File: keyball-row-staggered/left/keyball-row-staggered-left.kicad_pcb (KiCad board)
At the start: 2 copper layers, 159.2 x 113.7 mm, 82 parts, among them J1 MJ-4PP-9, J10 Conn_01x01_Pin, J11 Conn_01x01_Pin, J12 Conn_01x01_Pin, J2 Conn_01x01_Pin, J3 Conn_01x01_Pin, J4 Conn_01x01_Pin, J5 Conn_01x01_Pin, J6 Conn_01x01_Pin, J7 Conn_01x01_Pin, J8 Conn_01x01_Pin, J9 Conn_01x01_Pin, SW1 SW_PUSH, SW10 SW_PUSH, SW11 SW_PUSH, SW12 SW_PUSH, SW13 SW_PUSH, SW14 SW_PUSH, SW15 SW_PUSH, SW16 SW_PUSH, SW17 SW_PUSH, SW18 SW_PUSH, SW19 SW_PUSH, SW2 SW_PUSH, SW20 SW_PUSH, SW21 SW_PUSH, SW22 SW_PUSH, SW23 SW_PUSH, SW24 SW_PUSH, SW25 SW_PUSH, SW26 SW_PUSH, SW27 SW_PUSH, SW28 SW_PUSH, SW29 SW_PUSH, SW3 SW_PUSH, SW30 SW_PUSH, SW31 SW_PUSH, SW4 SW_PUSH, SW5 SW_PUSH, SW6 SW_PUSH, SW7 SW_PUSH, SW8 SW_PUSH, SW9 SW_PUSH, U1 ProMicro

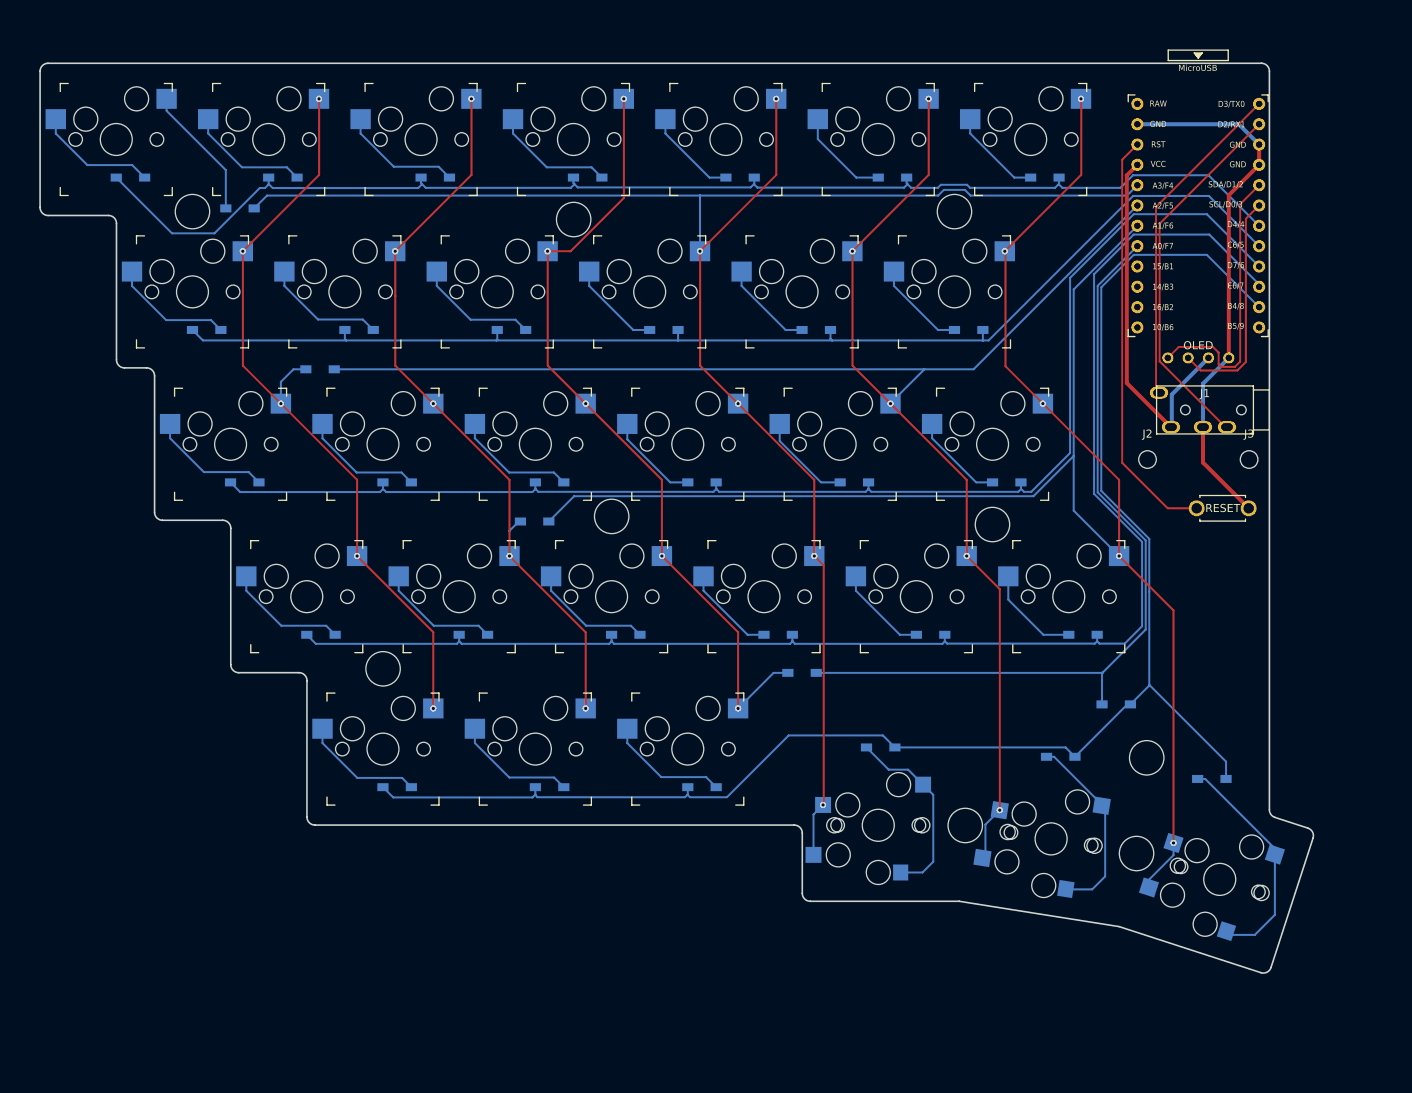
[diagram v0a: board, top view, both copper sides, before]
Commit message: add order-number placeholder
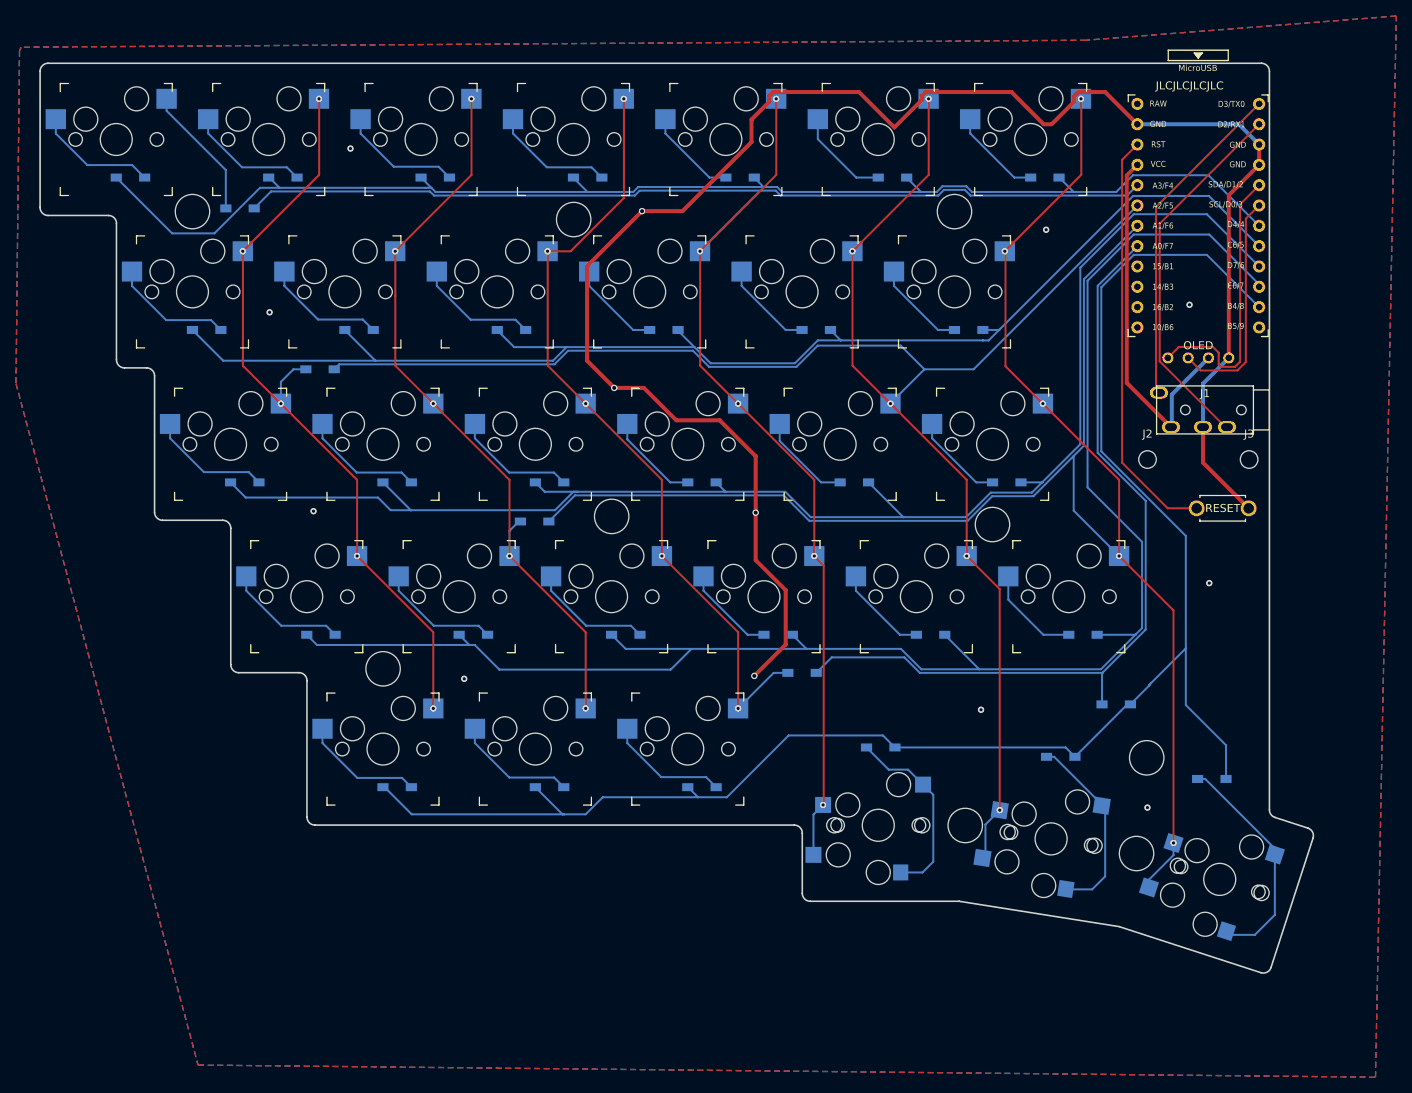
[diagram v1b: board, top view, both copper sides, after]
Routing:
- net GND: track 67.0 -> 224.7 mm, vias 0 -> 13
- net ROW3: track 183.2 -> 209.5 mm
- net ROW2: track 164.6 -> 184.8 mm
- net ROW1: track 150.7 -> 169.6 mm
- net ROW4: track 198.9 -> 211.7 mm
- net ROW0: track 159.1 -> 165.8 mm
- net COL0: track 224.5 -> 229.2 mm
- net COL1: track 222.3 -> 226.4 mm
- net COL2: track 228.5 -> 231.1 mm
- net COL3: track 99.9 -> 101.5 mm
- added copper zone on B.Cu, net GND
- added copper zone on F.Cu, net GND
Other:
- board text added: "JLCJLCJLCJLC"

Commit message: 発注ファイル作成
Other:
- board text removed: "JLCJLCJLCJLC"
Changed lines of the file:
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@@
     )
     (pad_to_mask_clearance 0)
+    (aux_axis_origin 19.05 133.063)
     (pcbplotparams
-      (layerselection 0x00010fc_ffffffff)
+      (layerselection 0x00010f0_ffffffff)
       (plot_on_all_layers_selection 0x0000000_00000000)
       (disableapertmacros false)
-      (usegerberextensions false)
+      (usegerberextensions true)
       (usegerberattributes true)
       (usegerberadvancedattributes true)
@@
       (outputformat 1)
       (mirror false)
-      (drillshape 1)
+      (drillshape 0)
       (scaleselection 1)
-      (outputdirectory "")
+      (outputdirectory "../elecrow/order/left/")
     )
   )
@@
   (gr_line (start 107.299999 40.625) (end 107.299999 54.625)
     (stroke (width 0.188976) (type solid)) (layer "User.1"))
-  (gr_text "JLCJLCJLCJLC" (at 158.5 22.44) (layer "F.SilkS")
-    (effects (font (size 1 1) (thickness 0.15)) (justify left bottom))
-  )
   (segment (start 111.0809 23.5109) (end 111.0809 33.0041) (width 0.25) (layer "F.Cu") (net 1))
   (segment (start 117 81.8175) (end 117 111.685) (width 0.25) (layer "F.Cu") (net 1))
